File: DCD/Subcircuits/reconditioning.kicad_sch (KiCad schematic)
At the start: 44 parts, among them IC1 830S21AMI-01LF, IC2 830S21AMI-01LF, U15 MC100EP31DTG, U16 MC100EP31DTG, U7 LP2985-33DBVR, U8 CDCLVC1104PWR, Y1 SiT8208AI-21-33E-50.000000

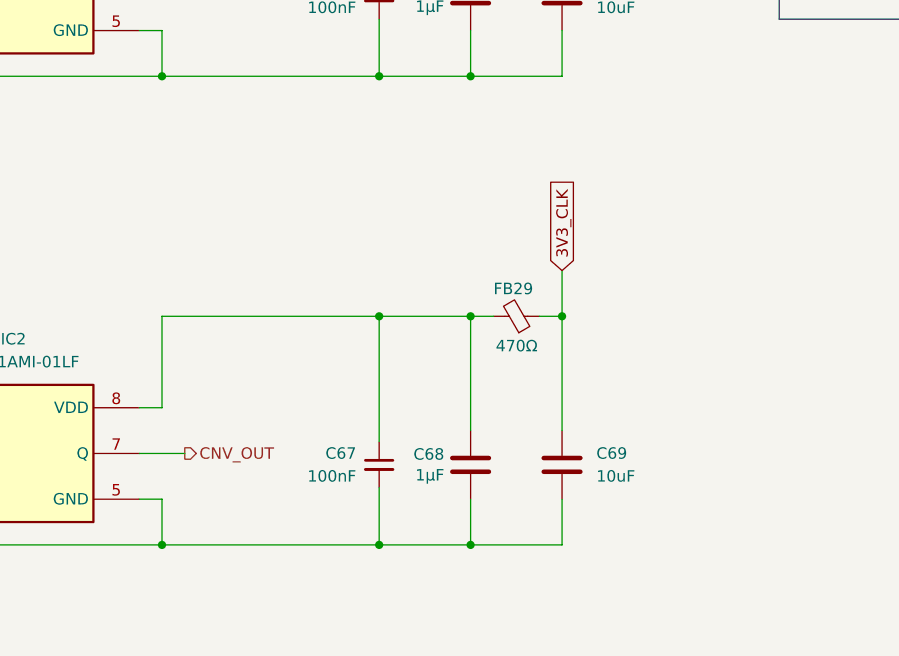
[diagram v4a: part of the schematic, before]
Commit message: Reduced the output voltage of the CNV reconditioned signal for the ADC
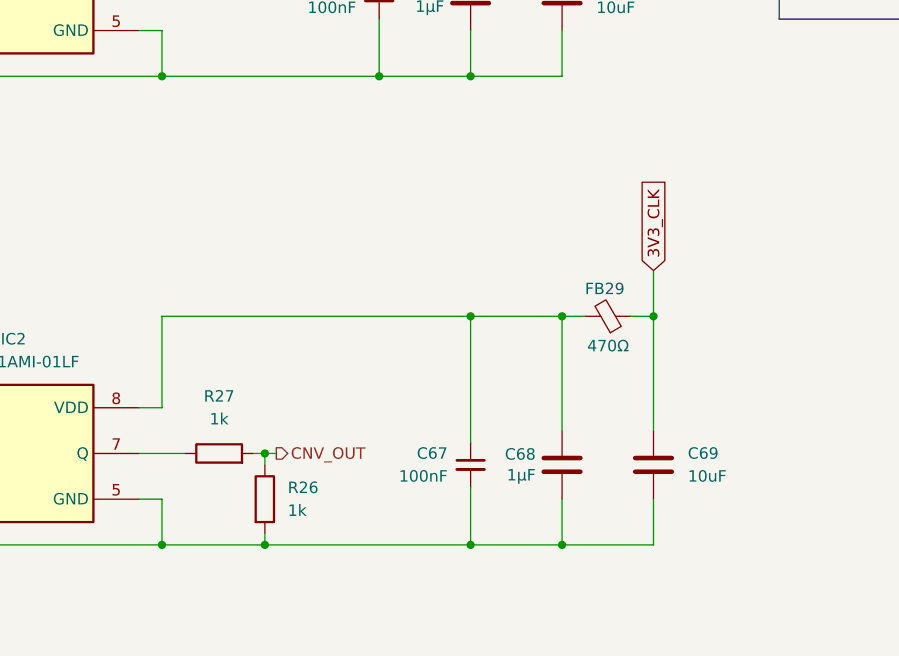
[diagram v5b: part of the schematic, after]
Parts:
- added R26, R27: 1k, symbol Device:R
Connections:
- net CNV_OUT: now also R26.1, R27.2; no longer IC2.7 (Q)
- net DGND: now also R26.2
- new net: IC2.7 (Q), R27.1
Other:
- moved on the sheet: C67, C68, C69, FB29
